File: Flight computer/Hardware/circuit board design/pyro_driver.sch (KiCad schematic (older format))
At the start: 16 parts, among them J3 Screw_Terminal_01x04, J5 Screw_Terminal_01x04, U5 Si7232DN, U6 Si7232DN

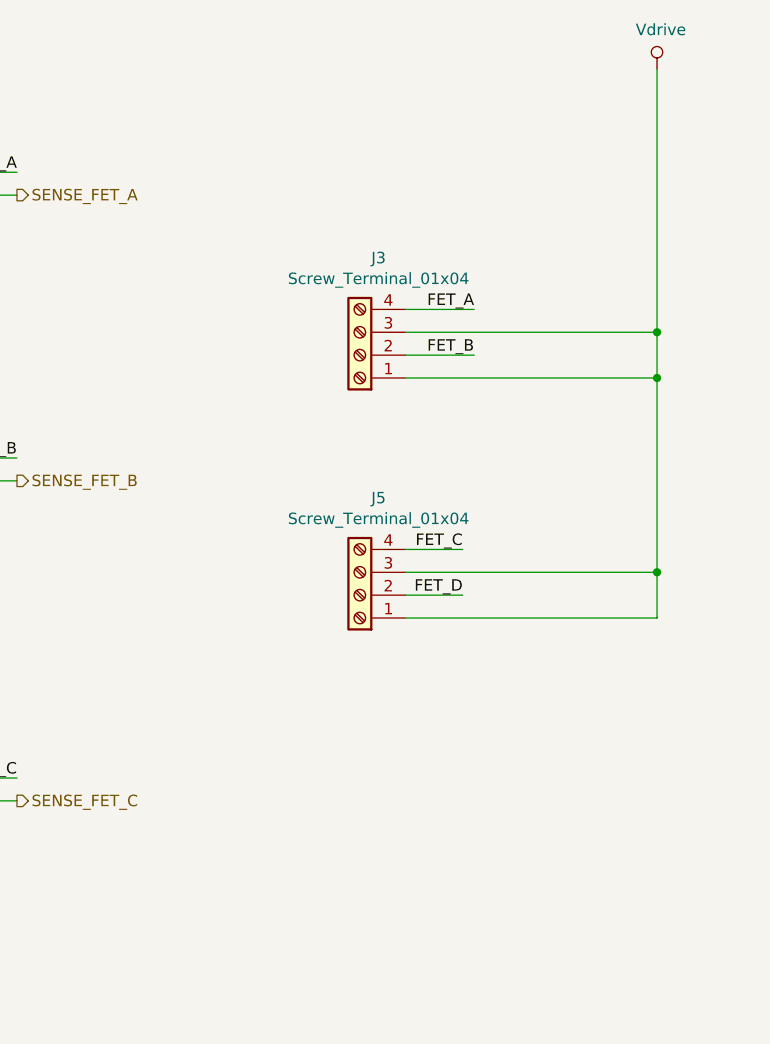
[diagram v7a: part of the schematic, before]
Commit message: added the arming switch. Changed foot print of lipo connector to JST
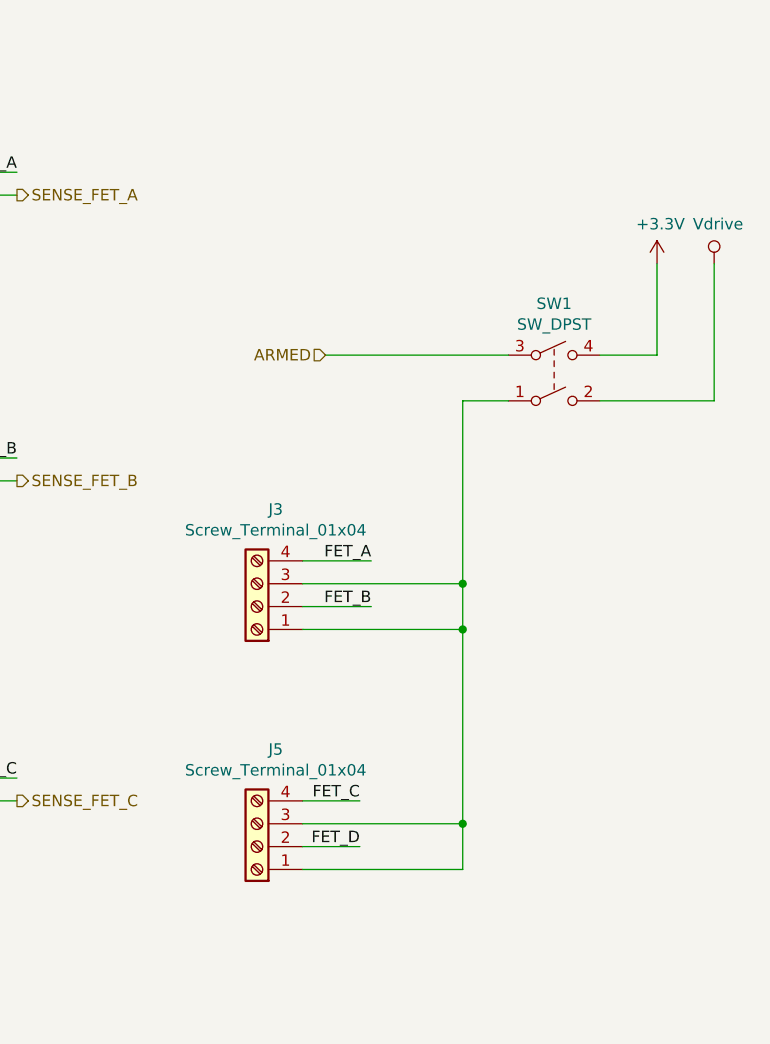
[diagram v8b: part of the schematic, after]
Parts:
- added SW1: SW_DPST, symbol Switch:SW_DPST
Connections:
- net Vdrive: now also SW1.2; no longer J3.1 (Pin_1), J3.3 (Pin_3), J5.1 (Pin_1), J5.3 (Pin_3)
- new net: J3.1 (Pin_1), J3.3 (Pin_3), J5.1 (Pin_1), J5.3 (Pin_3), SW1.1
- new net +3V3: SW1.4
- new net ARMED: SW1.3
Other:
- moved on the sheet: J3, J5
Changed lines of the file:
@@
 L Connector:Screw_Terminal_01x04 J?
 U 1 1 5D7D6AC3
-P 8950 2300
+P 8500 3400
 AR Path="/5D5B1705/5D7D6AC3" Ref="J?"  Part="1"
 AR Path="/5D6468D5/5D7D6AC3" Ref="J3"  Part="1"
-F 0 "J3" H 8868 1875 50  0000 C CNN
-F 1 "Screw_Terminal_01x04" H 8868 1966 50  0000 C CNN
-F 2 "TerminalBlock_TE-Connectivity:TerminalBlock_TE_282834-4_1x04_P2.54mm_Horizontal" H 8950 2300 50  0001 C CNN
-F 3 "~" H 8950 2300 50  0001 C CNN
-	1    8950 2300
+F 0 "J3" H 8418 2975 50  0000 C CNN
+F 1 "Screw_Terminal_01x04" H 8418 3066 50  0000 C CNN
+F 2 "TerminalBlock_TE-Connectivity:TerminalBlock_TE_282834-4_1x04_P2.54mm_Horizontal" H 8500 3400 50  0001 C CNN
+F 3 "~" H 8500 3400 50  0001 C CNN
+	1    8500 3400
 	-1   0    0    1
 $EndComp
@@
 L Connector:Screw_Terminal_01x04 J?
 U 1 1 5D7D6AC9
-P 8950 3350
+P 8500 4450
 AR Path="/5D5B1705/5D7D6AC9" Ref="J?"  Part="1"
 AR Path="/5D6468D5/5D7D6AC9" Ref="J5"  Part="1"
-F 0 "J5" H 8868 2925 50  0000 C CNN
-F 1 "Screw_Terminal_01x04" H 8868 3016 50  0000 C CNN
-F 2 "TerminalBlock_TE-Connectivity:TerminalBlock_TE_282834-4_1x04_P2.54mm_Horizontal" H 8950 3350 50  0001 C CNN
-F 3 "~" H 8950 3350 50  0001 C CNN
-	1    8950 3350
+F 0 "J5" H 8418 4025 50  0000 C CNN
+F 1 "Screw_Terminal_01x04" H 8418 4116 50  0000 C CNN
+F 2 "TerminalBlock_TE-Connectivity:TerminalBlock_TE_282834-4_1x04_P2.54mm_Horizontal" H 8500 4450 50  0001 C CNN
+F 3 "~" H 8500 4450 50  0001 C CNN
+	1    8500 4450
 	-1   0    0    1
 $EndComp
@@
 FET_D
 Wire Wire Line
-	9150 2200 10250 2200
+	8700 3300 9400 3300
 Wire Wire Line
-	10250 2200 10250 1050
+	8700 3500 9400 3500
 Wire Wire Line
-	9150 2400 10250 2400
+	9400 3500 9400 3300
+Connection ~ 9400 3300
+Connection ~ 9400 3500
 Wire Wire Line
-	10250 2400 10250 2200
-Connection ~ 10250 2200
-Connection ~ 10250 2400
+	8700 4350 9400 4350
 Wire Wire Line
-	9150 3250 10250 3250
+	9400 3500 9400 4350
 Wire Wire Line
-	10250 2400 10250 3250
+	8700 4550 9400 4550
 Wire Wire Line
-	9150 3450 10250 3450
-Wire Wire Line
-	10250 3450 10250 3250
-Connection ~ 10250 3250
-$Comp
-L power:Vdrive #PWR0112
-U 1 1 5D7E2F36
-P 10250 1050
-F 0 "#PWR0112" H 10050 900 50  0001 C CNN
-F 1 "Vdrive" H 10267 1223 50  0000 C CNN
-F 2 "" H 10250 1050 50  0001 C CNN
-F 3 "" H 10250 1050 50  0001 C CNN
-	1    10250 1050
-	1    0    0    -1
-$EndComp
-Text Label 9450 2100 2    50   ~ 0
+	9400 4550 9400 4350
+Connection ~ 9400 4350
+Text Label 9000 3200 2    50   ~ 0
 FET_A
 Wire Wire Line
-	9450 2100 9150 2100
-Text Label 9450 2300 2    50   ~ 0
+	9000 3200 8700 3200
+Text Label 9000 3400 2    50   ~ 0
 FET_B
 Wire Wire Line
-	9150 2300 9450 2300
-Text Label 9400 3150 2    50   ~ 0
+	8700 3400 9000 3400
+Text Label 8950 4250 2    50   ~ 0
 FET_C
 Wire Wire Line
-	9400 3150 9150 3150
-Text Label 9400 3350 2    50   ~ 0
+	8950 4250 8700 4250
+Text Label 8950 4450 2    50   ~ 0
 FET_D
 Wire Wire Line
-	9400 3350 9150 3350
+	8950 4450 8700 4450
 Wire Wire Line
 	4450 1800 5550 1800
@@
 Wire Wire Line
 	4450 5700 5550 5700
+$Comp
+L Switch:SW_DPST SW1
+U 1 1 5D8869C7
+P 9800 2400
+F 0 "SW1" H 9800 2725 50  0000 C CNN
+F 1 "SW_DPST" H 9800 2634 50  0000 C CNN
+F 2 "" H 9800 2400 50  0001 C CNN
+F 3 "~" H 9800 2400 50  0001 C CNN
+	1    9800 2400
+	1    0    0    -1
+$EndComp
+$Comp
+L power:Vdrive #PWR0112
+U 1 1 5D7E2F36
+P 10500 1900
+F 0 "#PWR0112" H 10300 1750 50  0001 C CNN
+F 1 "Vdrive" H 10517 2073 50  0000 C CNN
+F 2 "" H 10500 1900 50  0001 C CNN
+F 3 "" H 10500 1900 50  0001 C CNN
+	1    10500 1900
+	1    0    0    -1
+$EndComp
+Wire Wire Line
+	9400 2500 9600 2500
+Wire Wire Line
+	10000 2500 10500 2500
+Wire Wire Line
+	10500 2500 10500 1900
+Wire Wire Line
+	9400 2500 9400 3300
+Text HLabel 8800 2300 0    50   Input ~ 0
+ARMED
+Wire Wire Line
+	8800 2300 9600 2300
+Wire Wire Line
+	10000 2300 10250 2300
+Wire Wire Line
+	10250 2300 10250 1900
+$Comp
+L power:+3.3V #PWR0121
+U 1 1 5D89E3F1
+P 10250 1900
+F 0 "#PWR0121" H 10250 1750 50  0001 C CNN
+F 1 "+3.3V" H 10265 2073 50  0000 C CNN
+F 2 "" H 10250 1900 50  0001 C CNN
+F 3 "" H 10250 1900 50  0001 C CNN
+	1    10250 1900
+	1    0    0    -1
+$EndComp
 $EndSCHEMATC
